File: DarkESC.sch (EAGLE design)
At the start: 98 parts, among them IC1 7805DT, IC2 ACS712ELCTR-20A-T, Q1 BC817-40W, Q2 BC817-40W, Q3 BC817-40W, Q4 IRF520, Q5 IRF520, Q6 IRF520, Q7 IRF520, Q8 IRF520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

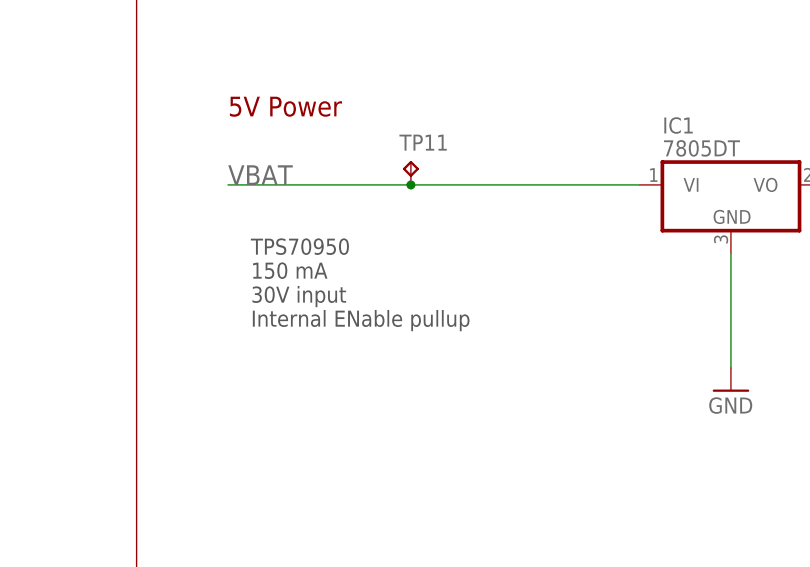
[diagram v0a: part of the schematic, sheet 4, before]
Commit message: Updated Power Lines
Updated Power Lines with Thicker Rails
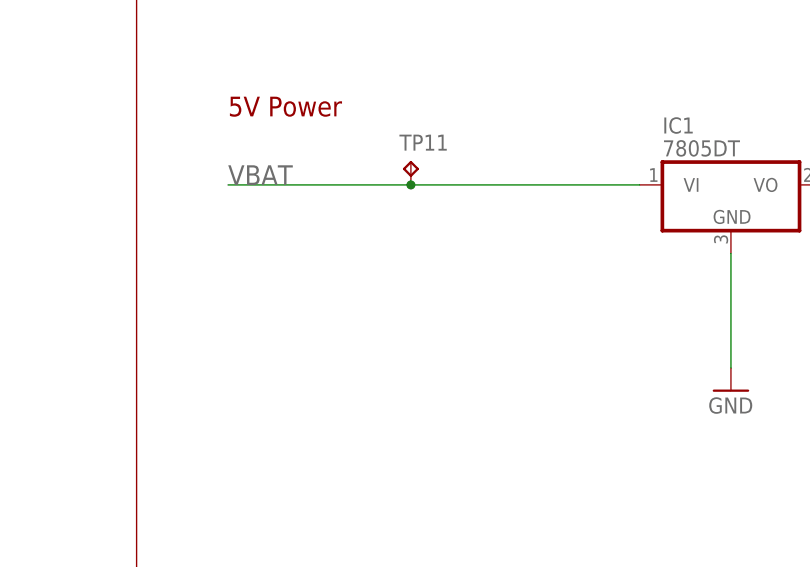
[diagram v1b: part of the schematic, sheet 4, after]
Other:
- note removed: "TPS70950 150 mA 30V input Internal ENable pullup"
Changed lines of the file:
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@@
 <text x="33.02" y="116.84" size="2.1844" layer="94">Power Decoupling</text>
 <text x="134.62" y="116.84" size="2.1844" layer="94">5V Power</text>
-<text x="137.16" y="93.472" size="1.778" layer="97">TPS70950
-150 mA
-30V input
-Internal ENable pullup</text>
 </plain>
 <instances>
@@
 </drawing>
 <compatibility>
-<note version="6.3" minversion="6.2.2" severity="warning">
-Since Version 6.2.2 text objects can contain more than one line,
-which will not be processed correctly with this version.
-</note>
 <note version="8.2" severity="warning">
 Since Version 8.2, EAGLE supports online libraries. The ids
